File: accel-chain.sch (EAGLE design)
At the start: 15 parts, among them IC1 ADXL330, IC2 ATTINY87/167AUTOMOTIVE, U1 ISL3179EIBZ

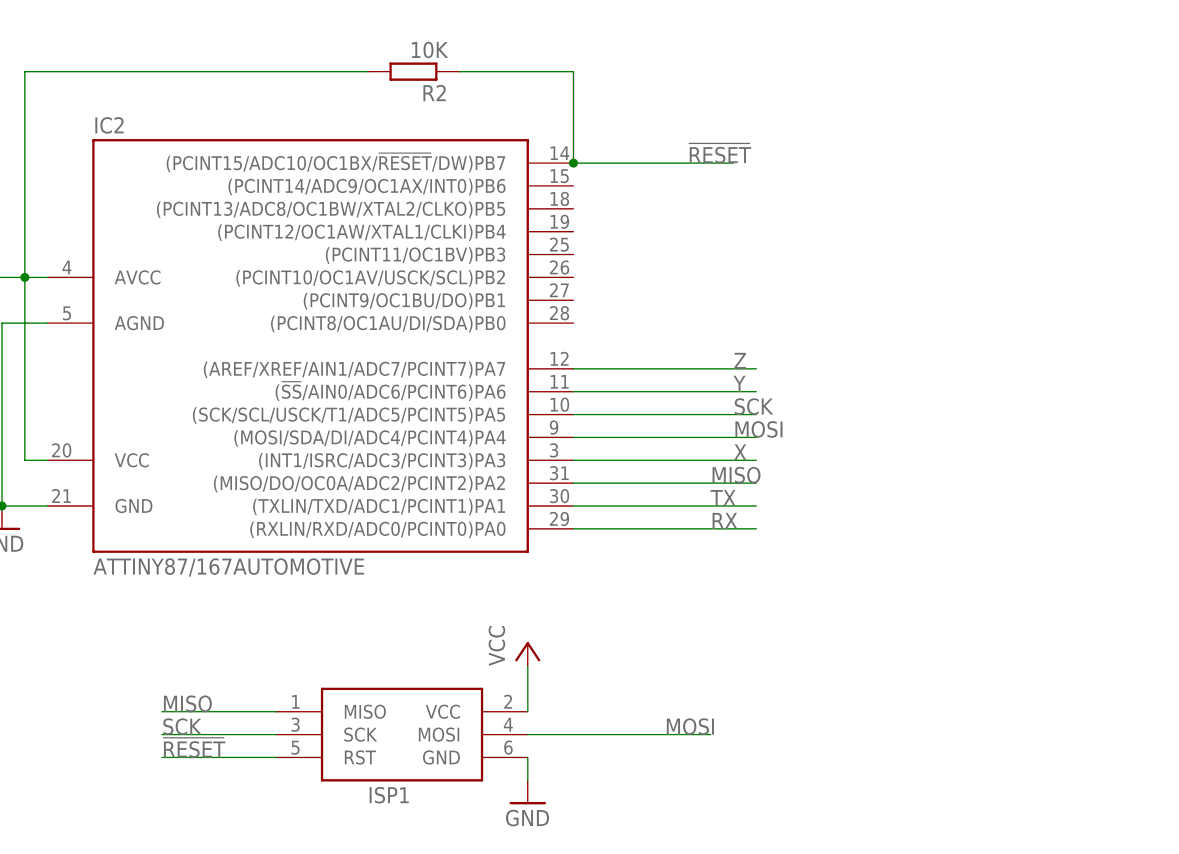
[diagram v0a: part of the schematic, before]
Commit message: Now with picoblade connectors
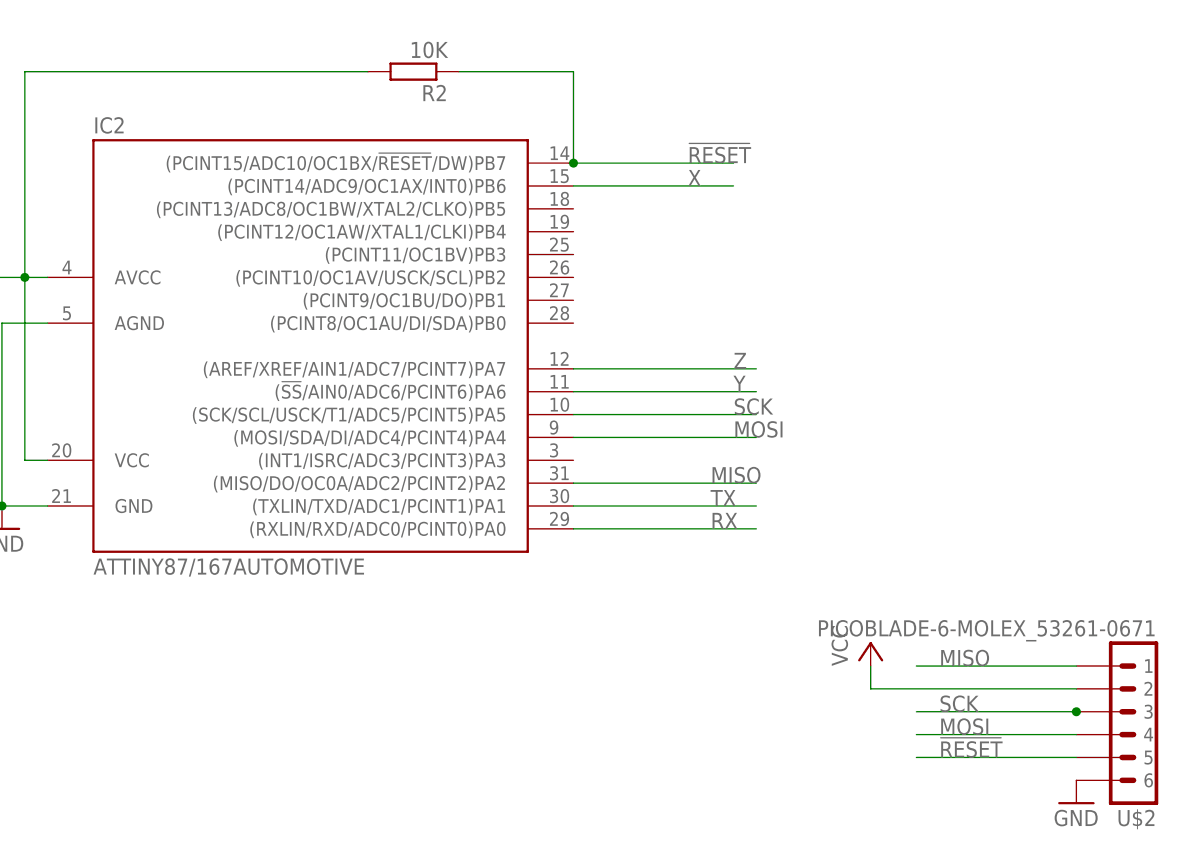
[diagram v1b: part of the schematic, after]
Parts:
- removed ISP1: AVRISP-6, adafruit:AVRISP-6
- added U$2: PICOBLADE-6-MOLEX_53261-0671, glacsweb:PICOBLADE-6-MOLEX_53261-0671
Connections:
- net !RESET: now also U$2.5; no longer ISP1.RST
- net GND: now also U$2.6; no longer ISP1.GND
- net MISO: now also U$2.1; no longer ISP1.MISO
- net MOSI: now also U$2.4; no longer ISP1.MOSI
- net SCK: now also U$2.3; no longer ISP1.SCK
- net VCC: now also U$2.2; no longer ISP1.VCC
- net X: now also IC2.(PCINT14/ADC9/OC1AX/INT0)PB6; no longer IC2.(INT1/ISRC/ADC3/PCINT3)PA3
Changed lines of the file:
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@@
 <part name="GND4" library="supply1" deviceset="GND" device=""/>
 <part name="R2" library="resistor" deviceset="R-EU_" device="R0805" value="10K"/>
-<part name="ISP1" library="adafruit" deviceset="AVRISP" device="-6"/>
-<part name="P+2" library="glacsweb" deviceset="VCC" device=""/>
-<part name="GND5" library="supply1" deviceset="GND" device=""/>
 <part name="JP1" library="pinhead" deviceset="PINHD-1X4" device=""/>
 <part name="JP2" library="pinhead" deviceset="PINHD-1X4" device=""/>
 <part name="GND6" library="supply1" deviceset="GND" device=""/>
 <part name="P+3" library="glacsweb" deviceset="VCC" device=""/>
+<part name="U$2" library="glacsweb" deviceset="PICOBLADE-6" device="-MOLEX_53261-0671"/>
+<part name="GND7" library="supply1" deviceset="GND" device=""/>
+<part name="P+4" library="glacsweb" deviceset="VCC" device=""/>
 </parts>
 <sheets>
@@
 <instance part="GND4" gate="1" x="106.68" y="66.04"/>
 <instance part="R2" gate="G$1" x="152.4" y="116.84" rot="R180"/>
-<instance part="ISP1" gate="G$1" x="149.86" y="43.18"/>
-<instance part="P+2" gate="VCC" x="165.1" y="53.34"/>
-<instance part="GND5" gate="1" x="165.1" y="35.56"/>
 <instance part="JP1" gate="A" x="71.12" y="43.18"/>
 <instance part="JP2" gate="A" x="40.64" y="43.18" rot="MR0"/>
 <instance part="GND6" gate="1" x="55.88" y="38.1"/>
 <instance part="P+3" gate="VCC" x="55.88" y="53.34"/>
+<instance part="U$2" gate="1" x="233.68" y="43.18" rot="R180"/>
+<instance part="GND7" gate="1" x="226.06" y="35.56"/>
+<instance part="P+4" gate="VCC" x="203.2" y="53.34"/>
 </instances>
 <busses>
@@
 </segment>
 <segment>
-<pinref part="ISP1" gate="G$1" pin="GND"/>
-<pinref part="GND5" gate="1" pin="GND"/>
-<wire x1="165.1" y1="40.64" x2="165.1" y2="38.1" width="0.1524" layer="91"/>
-</segment>
-<segment>
 <pinref part="JP2" gate="A" pin="4"/>
 <pinref part="JP1" gate="A" pin="4"/>
@@
 <wire x1="55.88" y1="40.64" x2="68.58" y2="40.64" width="0.1524" layer="91"/>
 <junction x="55.88" y="40.64"/>
+</segment>
+<segment>
+<pinref part="U$2" gate="1" pin="6"/>
+<pinref part="GND7" gate="1" pin="GND"/>
 </segment>
 </net>
@@
 </segment>
 <segment>
-<pinref part="IC2" gate="1" pin="(INT1/ISRC/ADC3/PCINT3)PA3"/>
-<wire x1="170.18" y1="73.66" x2="190.5" y2="73.66" width="0.1524" layer="91"/>
-<label x="187.96" y="73.66" size="1.778" layer="95"/>
+<pinref part="IC2" gate="1" pin="(PCINT14/ADC9/OC1AX/INT0)PB6"/>
+<wire x1="170.18" y1="104.14" x2="187.96" y2="104.14" width="0.1524" layer="91"/>
+<label x="182.88" y="104.14" size="1.778" layer="95"/>
 </segment>
 </net>
@@
 </segment>
 <segment>
-<pinref part="ISP1" gate="G$1" pin="VCC"/>
-<pinref part="P+2" gate="VCC" pin="VCC"/>
-<wire x1="165.1" y1="45.72" x2="165.1" y2="50.8" width="0.1524" layer="91"/>
-</segment>
-<segment>
 <pinref part="JP2" gate="A" pin="1"/>
 <pinref part="JP1" gate="A" pin="1"/>
@@
 <wire x1="55.88" y1="48.26" x2="55.88" y2="50.8" width="0.1524" layer="91"/>
 <junction x="55.88" y="48.26"/>
+</segment>
+<segment>
+<pinref part="U$2" gate="1" pin="2"/>
+<pinref part="P+4" gate="VCC" pin="VCC"/>
+<wire x1="226.06" y1="48.26" x2="203.2" y2="48.26" width="0.1524" layer="91"/>
+<wire x1="203.2" y1="48.26" x2="203.2" y2="50.8" width="0.1524" layer="91"/>
 </segment>
 </net>
@@
 </segment>
 <segment>
-<pinref part="ISP1" gate="G$1" pin="RST"/>
-<wire x1="137.16" y1="40.64" x2="124.46" y2="40.64" width="0.1524" layer="91"/>
-<label x="124.46" y="40.64" size="1.778" layer="95"/>
+<pinref part="U$2" gate="1" pin="5"/>
+<wire x1="226.06" y1="40.64" x2="208.28" y2="40.64" width="0.1524" layer="91"/>
+<label x="210.82" y="40.64" size="1.778" layer="95"/>
 </segment>
 </net>
@@
 </segment>
 <segment>
-<pinref part="ISP1" gate="G$1" pin="MOSI"/>
-<wire x1="165.1" y1="43.18" x2="185.42" y2="43.18" width="0.1524" layer="91"/>
-<label x="180.34" y="43.18" size="1.778" layer="95"/>
+<pinref part="U$2" gate="1" pin="4"/>
+<wire x1="226.06" y1="43.18" x2="208.28" y2="43.18" width="0.1524" layer="91"/>
+<label x="210.82" y="43.18" size="1.778" layer="95"/>
 </segment>
 </net>
@@
 </segment>
 <segment>
-<pinref part="ISP1" gate="G$1" pin="MISO"/>
-<wire x1="137.16" y1="45.72" x2="124.46" y2="45.72" width="0.1524" layer="91"/>
-<label x="124.46" y="45.72" size="1.778" layer="95"/>
+<pinref part="U$2" gate="1" pin="1"/>
+<wire x1="226.06" y1="50.8" x2="208.28" y2="50.8" width="0.1524" layer="91"/>
+<label x="210.82" y="50.8" size="1.778" layer="95"/>
 </segment>
 </net>
 <net name="SCK" class="0">
+<segment>
+<wire x1="226.06" y1="45.72" x2="208.28" y2="45.72" width="0.1524" layer="91"/>
+<label x="210.82" y="45.72" size="1.778" layer="95"/>
+<pinref part="U$2" gate="1" pin="3"/>
+<junction x="226.06" y="45.72"/>
+</segment>
 <segment>
 <pinref part="IC2" gate="1" pin="(SCK/SCL/USCK/T1/ADC5/PCINT5)PA5"/>
@@
 <label x="187.96" y="78.74" size="1.778" layer="95"/>
 </segment>
-<segment>
-<pinref part="ISP1" gate="G$1" pin="SCK"/>
-<wire x1="137.16" y1="43.18" x2="124.46" y2="43.18" width="0.1524" layer="91"/>
-<label x="124.46" y="43.18" size="1.778" layer="95"/>
-</segment>
-</net>
+</net>
